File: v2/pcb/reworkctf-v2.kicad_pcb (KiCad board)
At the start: 4 copper layers, 70 x 50 mm, 99 parts, among them J1 USB_C_Receptacle_USB2.0, J2 CORTEX_DEBUG_ETM, J6 CONN_01X03, J7 PMOD_HOST, J8 PMOD_HOST, M1 SCREWHOLE, M2 SCREWHOLE, M3 SCREWHOLE, M4 SCREWHOLE, U1 STM32H750XBH6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

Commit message: Got up to challenge 8
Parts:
- added J3: DOT, azonenberg_pcb:TESTPOINT_SMT_0.5MM, F.Cu at (49.3, 57.3)
- added R36: 10K, azonenberg_pcb:EIA_0201_RES_NOSILK, F.Cu at (53.6, 56.6)
- added R37: 10K, azonenberg_pcb:EIA_01005_RES_NOSILK, F.Cu at (54.4, 56.6)
- R17, R18, R19, R20, R21: moved to B.Cu
- moved R19 6.18 mm to (46.9, 63.6), turned to 0 degrees
- moved R18 5.19 mm to (46.9, 62.4), turned to 0 degrees
- moved R20 5.07 mm to (49.7, 64.0)
- moved R21 4.21 mm to (49.8, 62.4), turned to 180 degrees
- moved R17 1.36 mm to (44.3, 60.1), turned to 180 degrees
- turned D3 to 0 degrees
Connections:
- D3 pad 1: /GND -> Net-(D3-K)
- D3 pad 2: Net-(D3-A) -> /GND
- R12 pad 2: Net-(D3-A) -> Net-(D3-K)
- U1 pad T5: unconnected-(U1B-PB1-PadT5) -> /CHALLENGE_02_B
- U1 pad T7: unconnected-(U1F-PF11-PadT7) -> /CHALLENGE_08_A
- U1 pad U2: unconnected-(U1A-PA3-PadU2) -> /CHALLENGE_01
- U1 pad U3: unconnected-(U1A-PA4-PadU3) -> /CHALLENGE_02_A
- U1 pad U4: unconnected-(U1C-PC5-PadU4) -> /CHALLENGE_02_B
- U1 pad U5: unconnected-(U1B-PB0-PadU5) -> /CHALLENGE_02_A
- U1 pad U6: unconnected-(U1J-PJ3-PadU6) -> /CHALLENGE_04
- U1 pad U7: unconnected-(U1J-PJ4-PadU7) -> /CHALLENGE_05
- U1 pad U8: unconnected-(U1G-PG1-PadU8) -> /CHALLENGE_08_A
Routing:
- net /CHALLENGE_02_A: track 0.00 -> 14.2 mm
- net /CHALLENGE_02_B: track 0.00 -> 11.4 mm
- net /CHALLENGE_08_A: track 0.00 -> 7.69 mm
- net /QSPI_DQ2: track 23.6 -> 16.8 mm, vias 1 -> 2
- net /QSPI_DQ3: track 24.0 -> 17.7 mm, vias 1 -> 0
- net /CHALLENGE_01: track 0.00 -> 5.89 mm
- net /QSPI_DQ0: track 20.9 -> 15.1 mm, vias 1 -> 0
- net /QSPI_DQ1: track 20.3 -> 14.7 mm, vias 1 -> 2
- net /CHALLENGE_05: track 0.00 -> 3.00 mm
- net /CHALLENGE_04: track 0.00 -> 2.98 mm
- net /QSPI_CS_N: track 25.1 -> 22.9 mm
- net Net-(U4-WP#/IO2): track 3.66 -> 1.76 mm, vias 0 -> 1
- net /GND: track 352.0 -> 350.8 mm
- net Net-(U4-DI/IO0): track 3.14 -> 2.35 mm, vias 0 -> 1
- net Net-(D3-K): track 0.00 -> 0.75 mm
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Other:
- board text added: "<- CH03"
- board text added: "<- CH07"
- board text added: "CH01 ->"
- board text added: "CH02 ->"
- board text added: "CH04 ->"
- board text added: "CH05 ->"
- board text added: "CH08 ->"

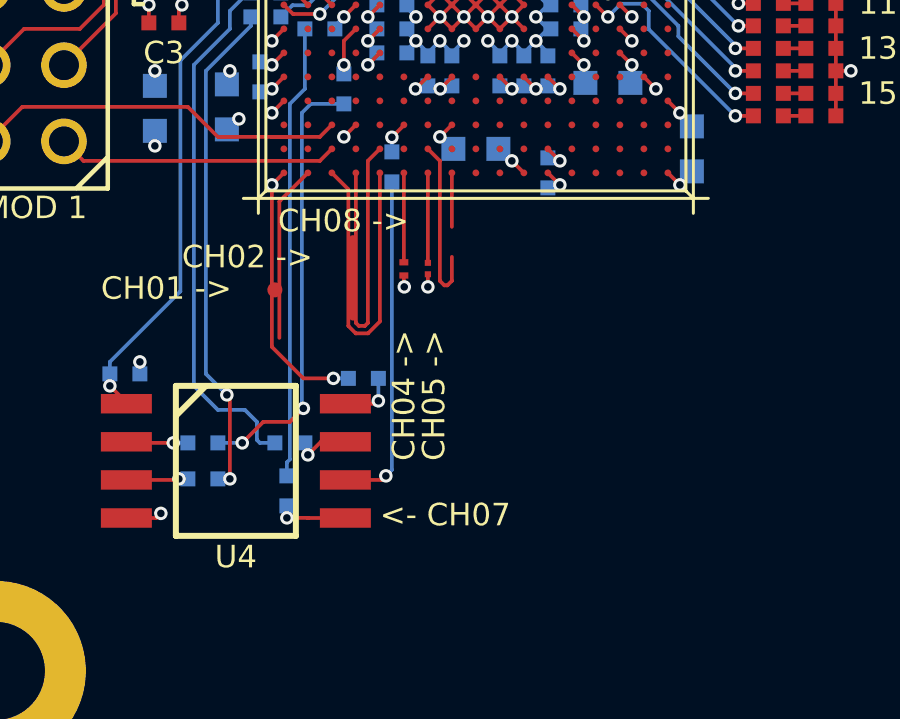
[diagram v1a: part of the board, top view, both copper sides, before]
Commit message: Added challenge 7 with lifted pad on the soic
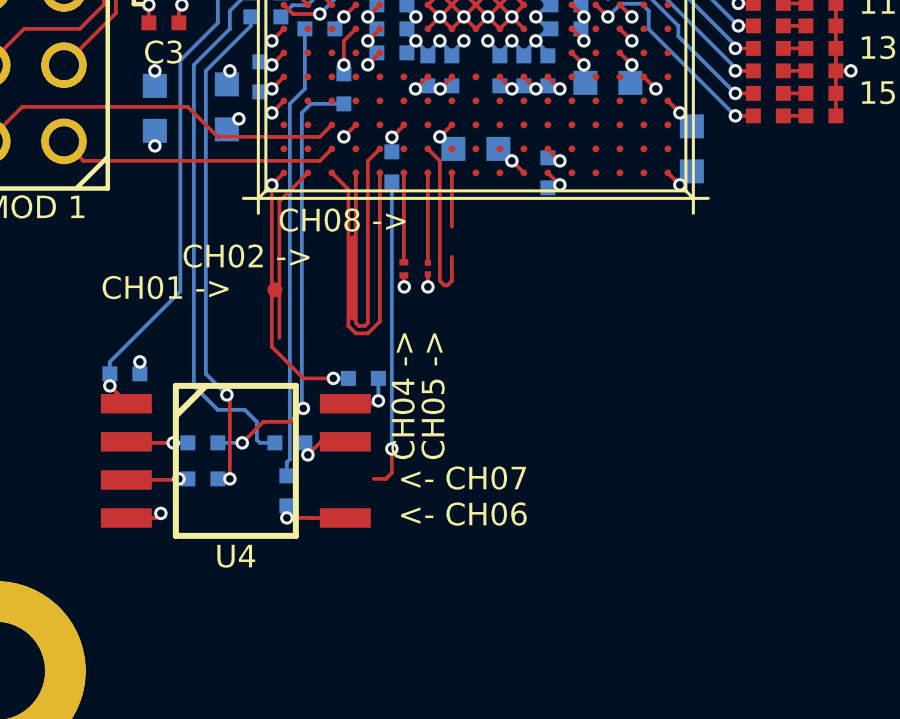
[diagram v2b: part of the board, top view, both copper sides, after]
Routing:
- net /QSPI_SCK: track 11.3 -> 10.4 mm
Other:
- board text added: "<- CH06"
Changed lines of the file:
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@@
 			(layer "F.SilkS")
 		)
+		(pad "" smd rect
+			(at 0.635 -3.65 270)
+			(size 0.65 1.7)
+			(layers "F.Mask")
+			(pinfunction "CLK")
+			(pintype "input")
+		)
 		(pad "1" smd rect
 			(at -1.905 3.65 270)
@@
 			(pintype "bidirectional")
 		)
-		(pad "6" smd rect
-			(at 0.635 -3.65 270)
-			(size 0.65 1.7)
-			(layers "F.Cu" "F.Mask" "F.Paste")
-			(net 43 "/QSPI_SCK")
-			(pinfunction "CLK")
-			(pintype "input")
-		)
 		(pad "7" smd rect
 			(at -0.635 -3.65 270)
@@
 	)
 	(gr_text "<- CH07"
-		(at 52.8 64.8 0)
+		(at 53.4 63.6 0)
+		(layer "F.SilkS")
+		(effects
+			(font
+				(size 0.75 0.75)
+				(thickness 0.1)
+			)
+			(justify left)
+		)
+	)
+	(gr_text "<- CH06"
+		(at 53.4 64.8 0)
 		(layer "F.SilkS")
 		(effects
@@
 	)
 	(segment
-		(start 51.65 63.635)
-		(end 52.865 63.635)
+		(start 53.2 62.6)
+		(end 53.2 63.4)
+		(width 0.125)
+		(layer "F.Cu")
+		(net 43)
+	)
+	(segment
+		(start 53.2 63.4)
+		(end 53 63.6)
 		(width 0.125)
 		(layer "F.Cu")
@@
 	)
 	(segment
-		(start 52.865 63.635)
-		(end 53 63.5)
+		(start 53 63.6)
+		(end 52.6 63.6)
 		(width 0.125)
 		(layer "F.Cu")
@@
 	)
 	(via
-		(at 53 63.5)
+		(at 53.2 62.6)
 		(size 0.45)
 		(drill 0.25)
@@
 	)
 	(segment
-		(start 53.2 63.3)
-		(end 53.2 53.699999)
-		(width 0.125)
-		(layer "B.Cu")
-		(net 43)
-	)
-	(segment
-		(start 53 63.5)
-		(end 53.2 63.3)
+		(start 53.2 53.699999)
+		(end 53.2 62.6)
 		(width 0.125)
 		(layer "B.Cu")

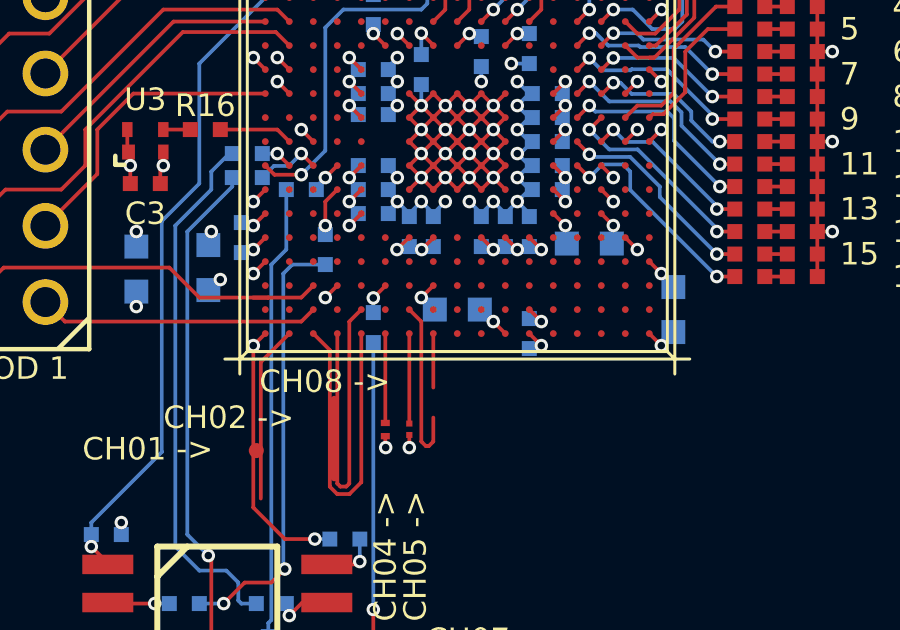
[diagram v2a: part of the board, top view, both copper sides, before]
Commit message: Added challenge 9 with diffpair polarity swap on inner layer
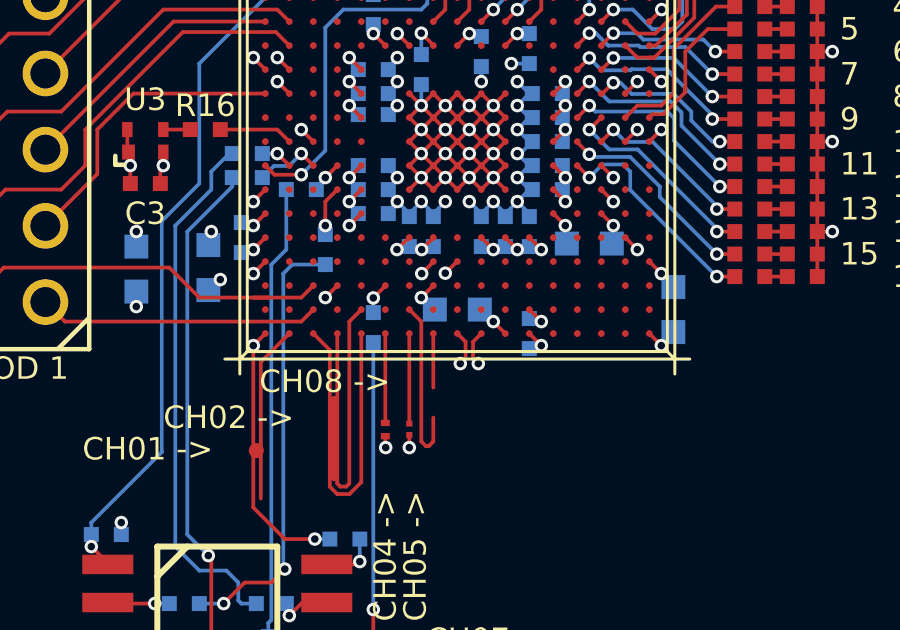
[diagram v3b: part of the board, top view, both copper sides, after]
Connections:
- U1 pad P8: unconnected-(U1F-PF14-PadP8) -> /CHALLENGE_09_N
- U1 pad P9: unconnected-(U1E-PE9-PadP9) -> /CHALLENGE_09_P
- U1 pad U10: unconnected-(U1E-PE14-PadU10) -> /CHALLENGE_09_P
- U1 pad U9: unconnected-(U1E-PE7-PadU9) -> /CHALLENGE_09_N
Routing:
- net /CHALLENGE_09_N: track 0.00 -> 18.2 mm, vias 0 -> 2
- net /CHALLENGE_09_P: track 0.00 -> 17.4 mm, vias 0 -> 2
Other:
- board text added: "<- CH09"

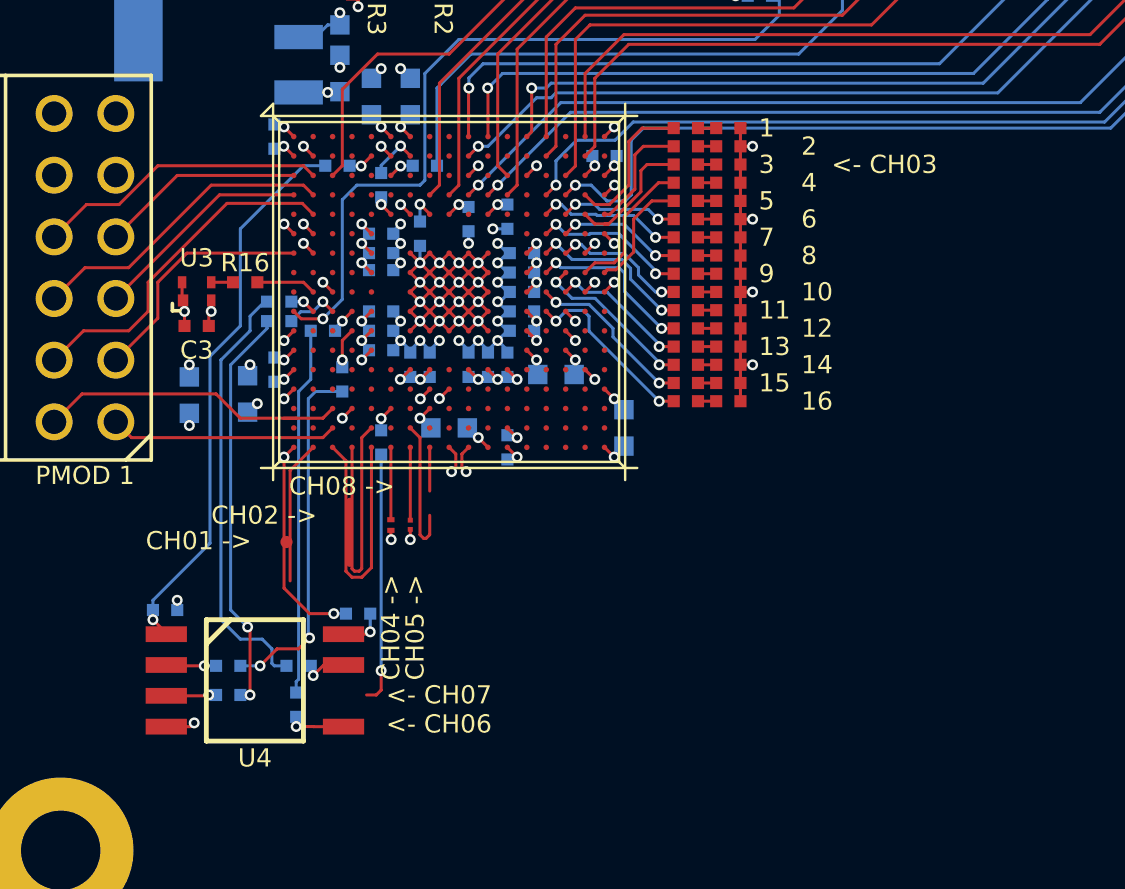
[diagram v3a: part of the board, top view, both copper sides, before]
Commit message: Added challenges 10 and 11 for vias
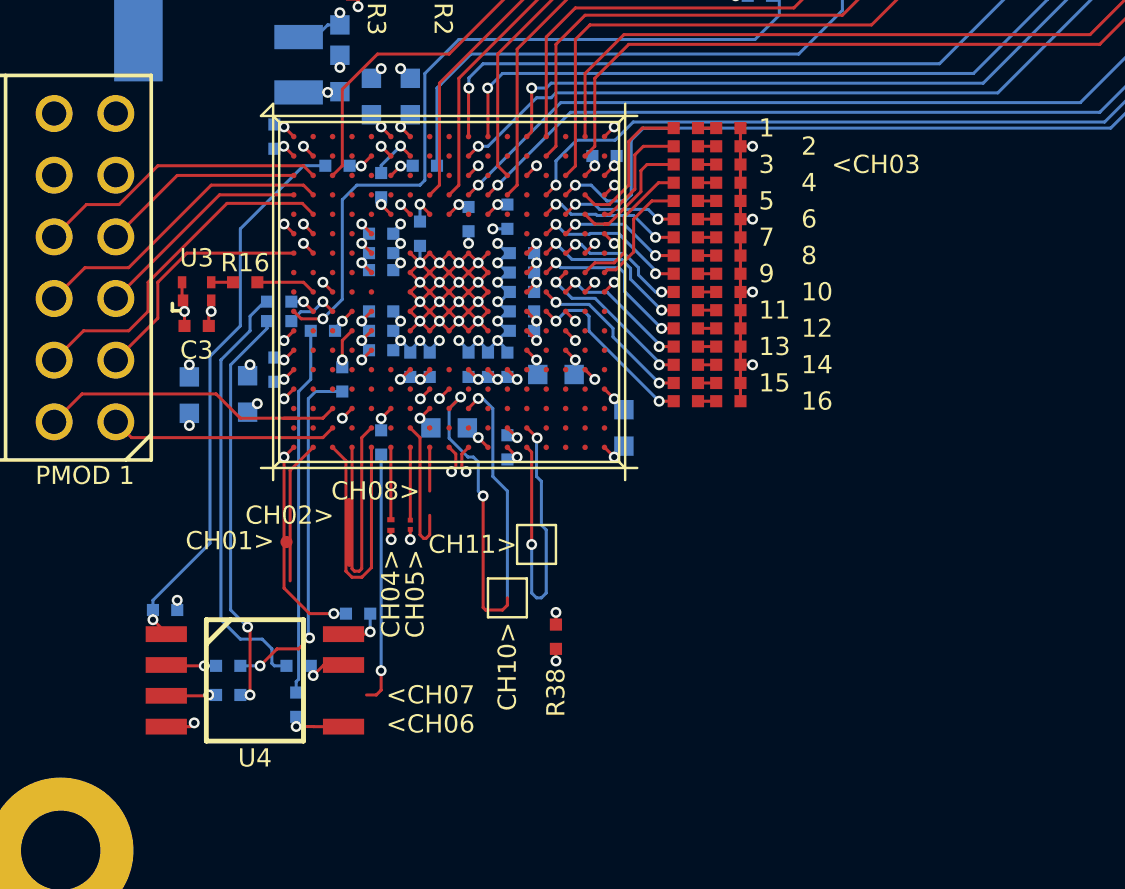
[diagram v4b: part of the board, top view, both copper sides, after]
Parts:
- added R38: 0, azonenberg_pcb:EIA_0402_RES_NOSILK, F.Cu at (60.4, 61.2)
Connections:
- U1 pad R10: unconnected-(U1E-PE12-PadR10) -> /CHALLENGE_10
- U1 pad R9: unconnected-(U1F-PF15-PadR9) -> /CHALLENGE_10
- U1 pad T13: unconnected-(U1H-PH8-PadT13) -> /CHALLENGE_11
- U1 pad U13: unconnected-(U1H-PH7-PadU13) -> /CHALLENGE_11
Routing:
- net /CHALLENGE_10: track 0.00 -> 21.1 mm, vias 0 -> 3
- net /CHALLENGE_11: track 0.00 -> 18.2 mm, vias 0 -> 3
- net /3V3: track 184.1 -> 194.8 mm, vias 35 -> 36
- added copper zone on In2.Cu, net /CHALLENGE_11
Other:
- board text added: "<CH03"
- board text added: "<CH06"
- board text added: "<CH07"
- board text added: "<CH09"
- board text added: "CH01>"
- board text added: "CH02>"
- board text added: "CH04>"
- board text added: "CH05>"
- board text added: "CH08>"
- board text added: "CH10>"
- board text added: "CH11>"
- board text removed: "<- CH03"
- board text removed: "<- CH06"
- board text removed: "<- CH07"
- board text removed: "<- CH09"
- board text removed: "CH01 ->"
- board text removed: "CH02 ->"
- board text removed: "CH04 ->"
- board text removed: "CH05 ->"
- board text removed: "CH08 ->"

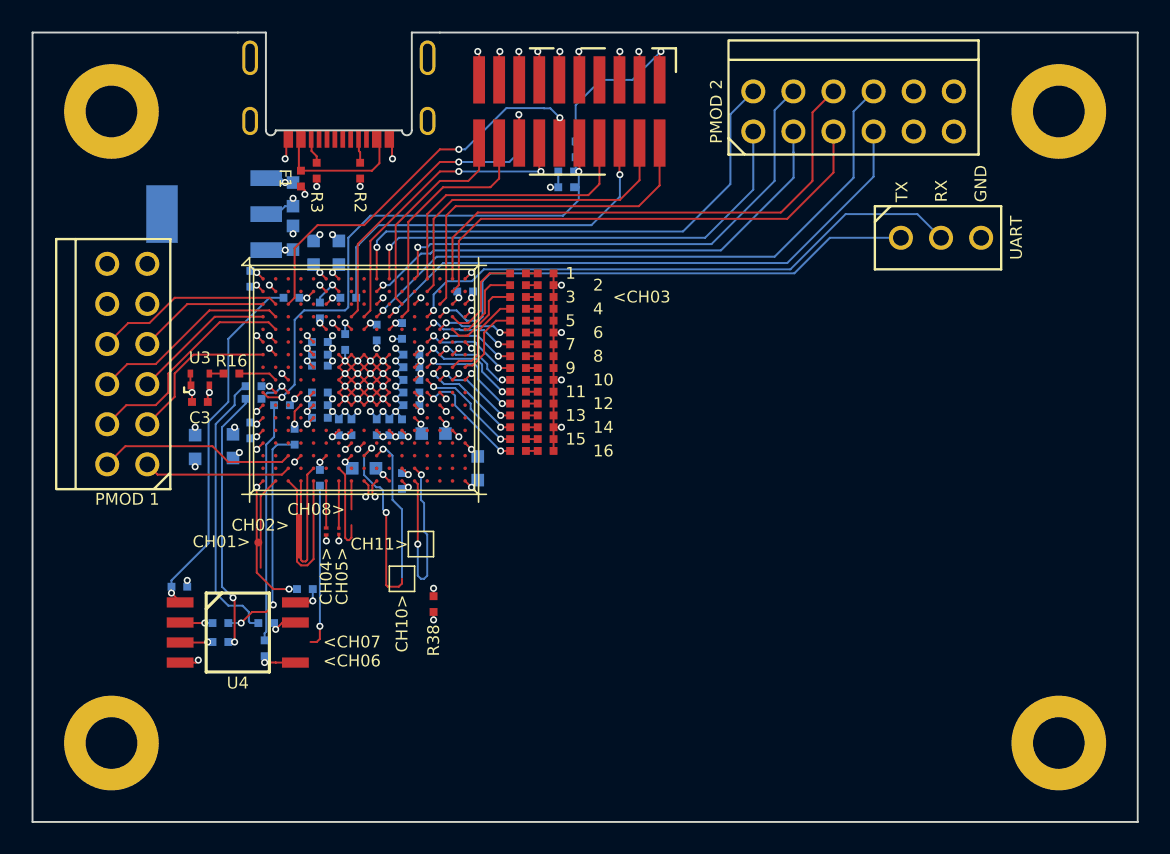
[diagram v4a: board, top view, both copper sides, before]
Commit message: Added SM-2 challenge, shrunk overall PCB footprint a bunch
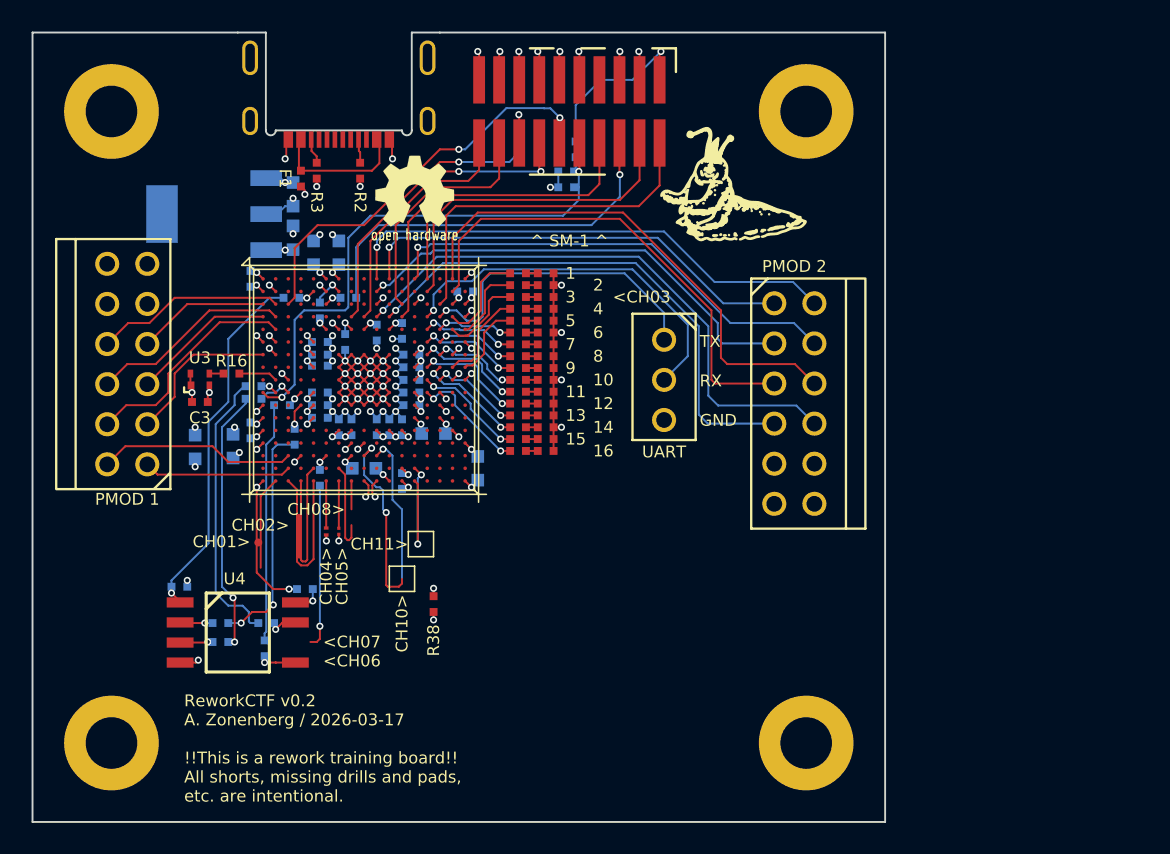
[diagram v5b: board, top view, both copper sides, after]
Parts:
- added M5: OSHW, w_logo:Logo_silk_OSHW_6x6mm, F.Cu at (59.2, 35.0)
- added M6: LONGTHING, azonenberg_pcb:LONGTHING-1200DPI, F.Cu at (79.9, 35.0)
- moved J6 19.7 mm to (75.0, 47.0), turned to -90 degrees
- moved J7 18.9 mm to (83.2, 48.5), turned to 90 degrees
- moved M3 16.0 mm to (84.0, 30.0)
- moved M4 16.0 mm to (84.0, 70.0)
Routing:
- net /UART_TX: track 33.1 -> 19.9 mm
- net /UART_RX: track 36.4 -> 23.9 mm
- net /GND: track 350.8 -> 338.7 mm
- net /3V3: track 194.8 -> 201.3 mm
- net /CHALLENGE_11: track 18.2 -> 13.3 mm
- net /PMOD2_DQ3: track 37.2 -> 33.3 mm
- net /PMOD2_DQ7: track 39.8 -> 36.2 mm
- net /PMOD2_DQ1: track 32.3 -> 29.3 mm
- net /PMOD2_DQ5: track 32.6 -> 29.9 mm
- net /PMOD2_DQ0: track 30.3 -> 28.4 mm
- net /PMOD2_DQ6: track 33.1 -> 32.4 mm
- net /PMOD2_DQ2: track 31.5 -> 30.8 mm
- net /PMOD2_DQ4: track 32.8 -> 32.3 mm
- added copper zone on In2.Cu, net /3V3
- added copper zone on In1.Cu, net /GND
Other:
- board size 70 x 50 mm -> 54 x 50 mm
- board text added: "<SM-2"
- board text added: "ReworkCTF v0.2 A. Zonenberg / 2026-03-17 !!This is a rework training board!! All shorts, missing drills and pads, etc. are intentional."
- board text added: "^ SM-1 ^"

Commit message: Added challenge 15 (missing pullup)
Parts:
- added J4: TESTPOINT, azonenberg_pcb:TESTPOINT_SMT_0.5MM, F.Cu at (49.6, 38.2)
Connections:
- U1 pad A2: unconnected-(U1I-PI6-PadA2) -> /CHALLENGE_12
- U1 pad A3: unconnected-(U1I-PI5-PadA3) -> /CHALLENGE_12
- U1 pad E3: unconnected-(U1C-PC13-PadE3) -> /CHALLENGE_15
- U1 pad P11: unconnected-(U1B-PB10-PadP11) -> /CHALLENGE_14
- U1 pad R13: unconnected-(U1H-PH9-PadR13) -> /CHALLENGE_14
- U1 pad T14: unconnected-(U1B-PB12-PadT14) -> /CHALLENGE_13
- U1 pad U14: unconnected-(U1B-PB13-PadU14) -> /CHALLENGE_13
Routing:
- net /CHALLENGE_12: track 0.00 -> 3.53 mm
- net /CHALLENGE_15: track 0.00 -> 2.97 mm, vias 0 -> 1
- net /CHALLENGE_14: track 0.00 -> 1.70 mm, vias 0 -> 2
- net /CHALLENGE_13: track 0.00 -> 1.37 mm, vias 0 -> 2
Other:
- board text added: "CH12>"
